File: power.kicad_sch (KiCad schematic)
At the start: 41 parts, among them IC1 TPS630702RNMR, J1 USB_C_Receptacle_USB2.0_16P, J8 1053141104, U3 L6983NQTR

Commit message: aggiornamenti rev 1.1
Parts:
- L2: footprint Inductor_SMD:L_1206_3216Metric_Pad1.42x1.75mm_HandSolder -> Inductor_SMD:L_1008_2520Metric
- USB1: footprint usb_c:USB-C-TH_TYPEC-306DDW-ARP16 -> BXCONN UC23-0B16F00P11:USB-C-TH_UC23-0B16F00P11
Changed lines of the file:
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@@
 			)
 		)
-		(property "Footprint" "usb_c:USB-C-TH_TYPEC-306DDW-ARP16"
+		(property "Footprint" "BXCONN UC23-0B16F00P11:USB-C-TH_UC23-0B16F00P11"
 			(at 236.22 153.67 0)
 			(effects
@@
 			)
 		)
-		(property "Footprint" "Inductor_SMD:L_1206_3216Metric_Pad1.42x1.75mm_HandSolder"
+		(property "Footprint" "Inductor_SMD:L_1008_2520Metric"
 			(at 105.41 105.41 0)
 			(effects

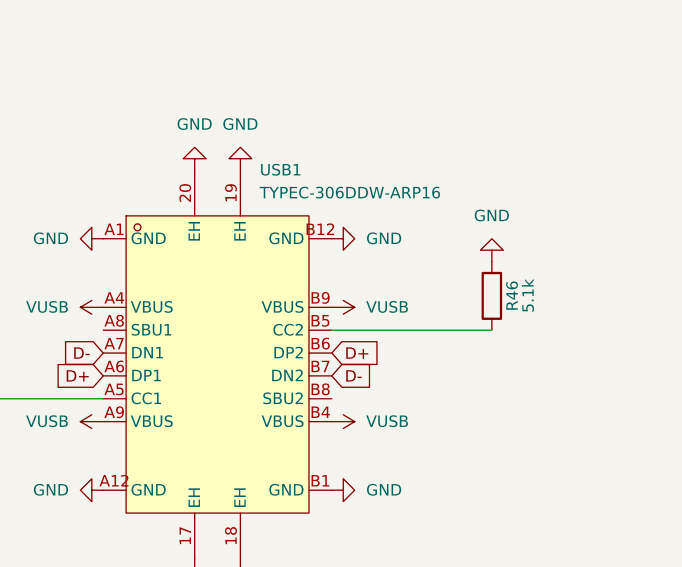
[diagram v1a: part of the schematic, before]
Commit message: nuovo routing completato (piste 0.15mm)
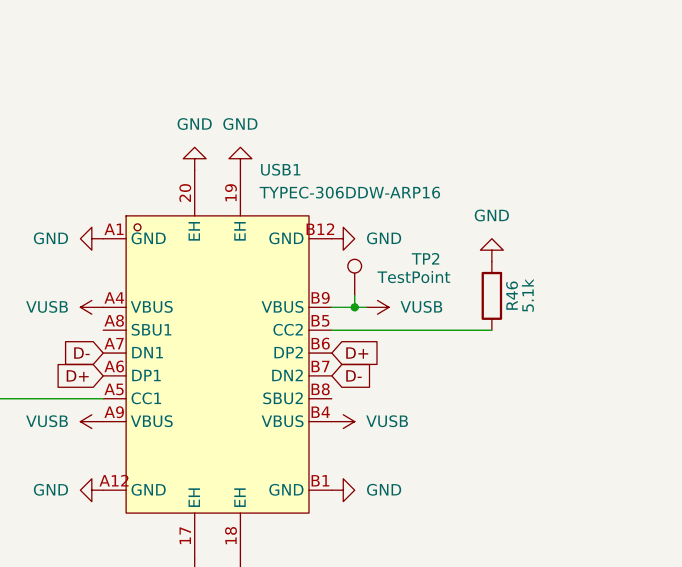
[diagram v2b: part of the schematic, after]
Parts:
- added TP2: TestPoint, TestPoint:TestPoint_Pad_2.0x2.0mm, symbol Connector:TestPoint
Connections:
- net VUSB: now also TP2.1
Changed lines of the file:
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@@
 	)
 	(junction
+		(at 251.46 118.11)
+		(diameter 0)
+		(color 0 0 0 0)
+	)
+	(junction
 		(at 43.18 154.94)
 		(diameter 0)
@@
 	(wire
 		(pts
+			(xy 251.46 118.11) (xy 248.92 118.11)
+		)
+		(stroke
+			(width 0)
+			(type default)
+		)
+	)
+	(wire
+		(pts
 			(xy 67.31 43.18) (xy 97.79 43.18)
 		)
@@
 	(wire
 		(pts
+			(xy 252.73 118.11) (xy 251.46 118.11)
+		)
+		(stroke
+			(width 0)
+			(type default)
+		)
+	)
+	(wire
+		(pts
 			(xy 46.99 30.48) (xy 46.99 31.75)
 		)
@@
 	(wire
 		(pts
+			(xy 251.46 116.84) (xy 251.46 118.11)
+		)
+		(stroke
+			(width 0)
+			(type default)
+		)
+	)
+	(wire
+		(pts
 			(xy 85.09 115.57) (xy 91.44 115.57)
 		)
@@
 	(symbol
 		(lib_id "power:+5V")
-		(at 248.92 118.11 270)
+		(at 252.73 118.11 270)
 		(unit 1)
 		(exclude_from_sim no)
@@
 		(fields_autoplaced yes)
 		(property "Reference" "#PWR0131"
-			(at 245.11 118.11 0)
+			(at 248.92 118.11 0)
 			(effects
 				(font
@@
 		)
 		(property "Value" "VUSB"
-			(at 252.73 118.1099 90)
+			(at 256.54 118.1099 90)
 			(effects
 				(font
@@
 		)
 		(property "Footprint" ""
-			(at 248.92 118.11 0)
+			(at 252.73 118.11 0)
 			(effects
 				(font
@@
 		)
 		(property "Datasheet" ""
-			(at 248.92 118.11 0)
+			(at 252.73 118.11 0)
 			(effects
 				(font
@@
 		)
 		(property "Description" "Power symbol creates a global label with name \"+5V\""
-			(at 248.92 118.11 0)
+			(at 252.73 118.11 0)
 			(effects
 				(font
@@
 					(unit 1)
 				)
+			)
+		)
+	)
+	(symbol
+		(lib_id "Connector:TestPoint")
+		(at 251.46 116.84 0)
+		(unit 1)
+		(exclude_from_sim no)
+		(in_bom yes)
+		(on_board yes)
+		(dnp no)
+		(property "Reference" "TP2"
+			(at 257.81 112.776 0)
+			(effects
+				(font
+					(size 1.27 1.27)
+				)
+				(justify left)
+			)
+		)
+		(property "Value" "TestPoint"
+			(at 254 114.8079 0)
+			(effects
+				(font
+					(size 1.27 1.27)
+				)
+				(justify left)
+			)
+		)
+		(property "Footprint" "TestPoint:TestPoint_Pad_2.0x2.0mm"
+			(at 256.54 116.84 0)
+			(effects
+				(font
+					(size 1.27 1.27)
+				)
+				(hide yes)
+			)
+		)
+		(property "Datasheet" "~"
+			(at 256.54 116.84 0)
+			(effects
+				(font
+					(size 1.27 1.27)
+				)
+				(hide yes)
+			)
+		)
+		(property "Description" "test point"
+			(at 251.46 116.84 0)
+			(effects
+				(font
+					(size 1.27 1.27)
+				)
+				(hide yes)
+			)
+		)
+		(pin "1"
+		)
+		(instances
+			(project ""
+				(path "/105f6e80-8e20-4d56-8eb3-6fa826818670/9d5abf06-99d5-4fb2-96aa-935d57e25668"
+					(reference "TP2")
+					(unit 1)
+				)

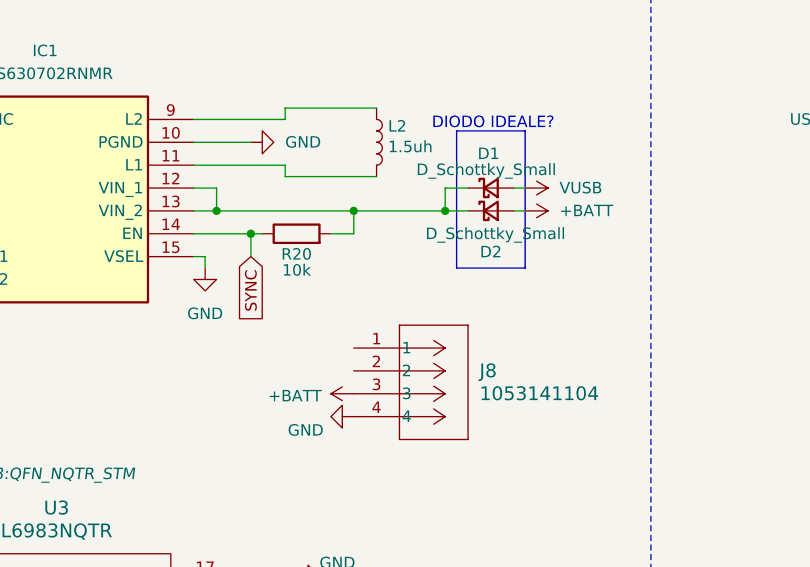
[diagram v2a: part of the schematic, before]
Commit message: TPS cap added
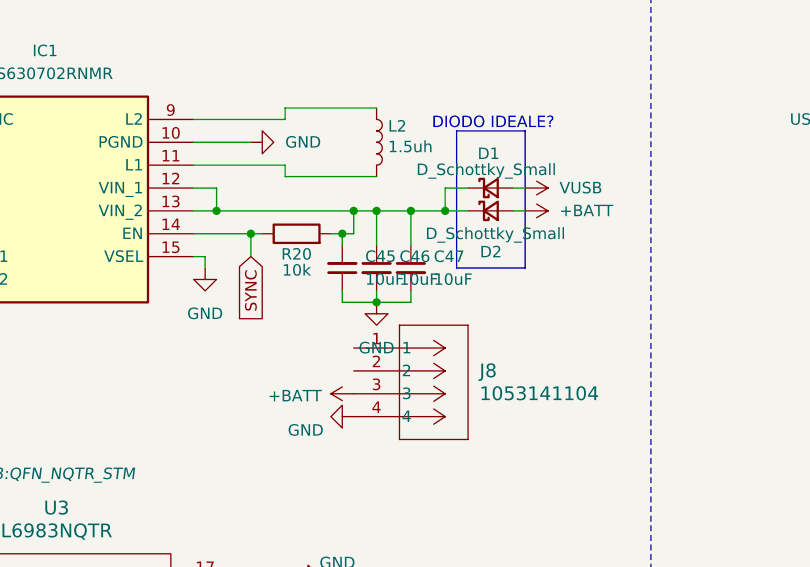
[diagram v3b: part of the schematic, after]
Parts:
- added C45, C46, C47: 10uF, Capacitor_SMD:C_0603_1608Metric_Pad1.08x0.95mm_HandSolder, symbol Device:C_Small
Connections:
- net GND: now also C45.1, C46.2, C47.2
- net at D1.1 (K), D2.1 (K), IC1.12 (VIN_1)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: now also C45.2, C46.1, C47.1
